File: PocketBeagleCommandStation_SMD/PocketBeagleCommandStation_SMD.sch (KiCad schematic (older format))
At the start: 37 parts, among them J1 Console, J2 DCC Output to Tracks, J7 USB_A, P1 POCKETBEAGLE-P1, P2 POCKETBEAGLE-P2, T1 DCC Power In, U11 INA2180A1IDGKR

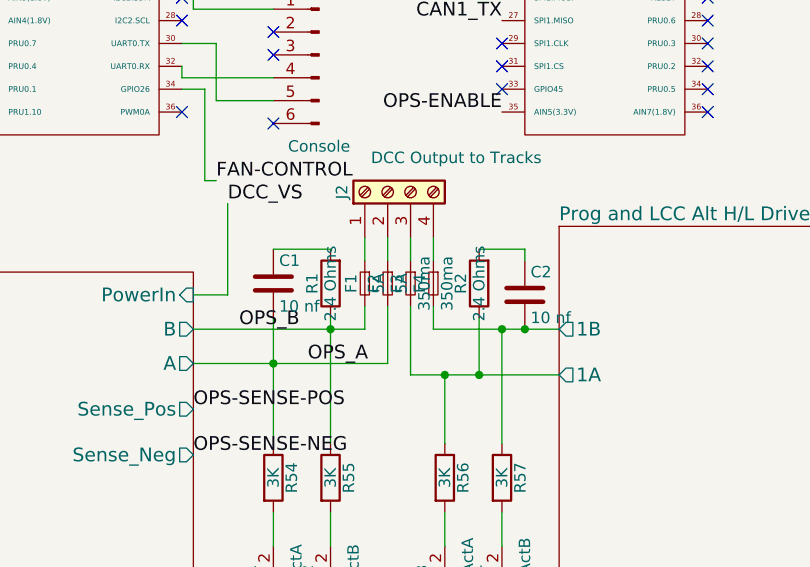
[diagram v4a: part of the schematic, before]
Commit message: continuing work on PocketBeagleCommandStation_SMD.
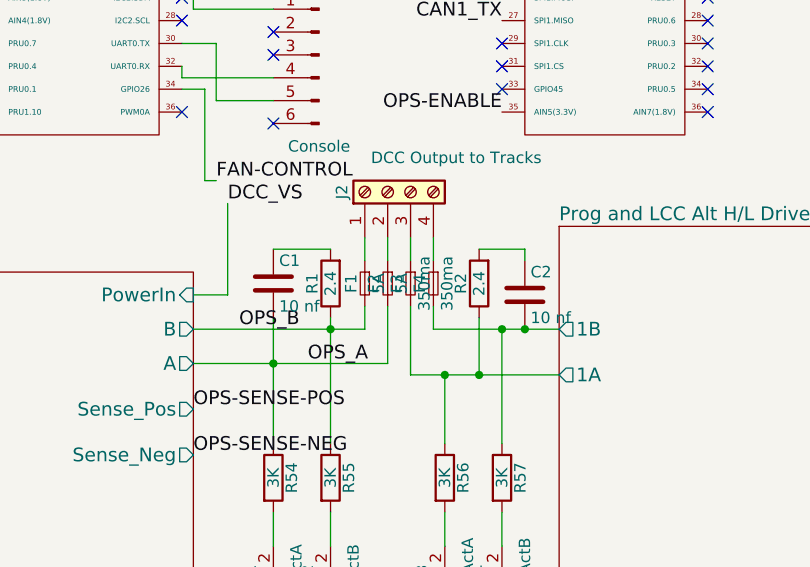
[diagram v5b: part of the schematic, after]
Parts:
- R1, R2: value 2.4 Ohms -> 2.4; footprint Resistors_THT:R_Axial_DIN0204_L3.6mm_D1.6mm_P2.54mm_Vertical -> Resistors_SMD:R_1206; Part Number 603-CFR-25JB-52-2R4 -> 71-CRCW12062R40FKEA
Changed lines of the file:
@@
 P 3950 4100
 F 0 "R1" V 4030 4100 50  0000 C CNN
-F 1 "2.4 Ohms" V 3950 4100 50  0000 C CNN
-F 2 "Resistors_THT:R_Axial_DIN0204_L3.6mm_D1.6mm_P2.54mm_Vertical" V 3880 4100 50  0001 C CNN
+F 1 "2.4" V 3950 4100 50  0000 C CNN
+F 2 "Resistors_SMD:R_1206" V 3880 4100 50  0001 C CNN
 F 3 "" H 3950 4100 50  0001 C CNN
-F 4 "603-CFR-25JB-52-2R4" V 3950 4100 60  0001 C CNN "Part Number"
+F 4 "71-CRCW12062R40FKEA" V 3950 4100 60  0001 C CNN "Part Number"
 	1    3950 4100
 	-1   0    0    1
@@
 P 4600 4100
 F 0 "R2" V 4680 4100 50  0000 C CNN
-F 1 "2.4 Ohms" V 4600 4100 50  0000 C CNN
-F 2 "Resistors_THT:R_Axial_DIN0204_L3.6mm_D1.6mm_P2.54mm_Vertical" V 4530 4100 50  0001 C CNN
+F 1 "2.4" V 4600 4100 50  0000 C CNN
+F 2 "Resistors_SMD:R_1206" V 4530 4100 50  0001 C CNN
 F 3 "" H 4600 4100 50  0001 C CNN
-F 4 "603-CFR-25JB-52-2R4" V 4600 4100 60  0001 C CNN "Part Number"
+F 4 "71-CRCW12062R40FKEA" V 4600 4100 60  0001 C CNN "Part Number"
 	1    4600 4100
 	-1   0    0    1

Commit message: Continuing work on PocketBeagleCommandStation_SMD.
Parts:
- added FID1, FID2, FID3: Fiducial, Fiducials:Fiducial_Modern_CopperTop, symbol Mounting_Hole
- added MK1, MK3, MK4: Mounting_Hole, Mounting_Holes:MountingHole_3.2mm_M3, symbol Mounting_Hole
- added MK2: Mounting_Hole_PAD, Mounting_Holes:MountingHole_3.2mm_M3_Pad_Via, symbol Mounting_Hole_PAD
- R48: footprint (none) -> Resistors_SMD:R_0603; Mouser Part Number (none) -> 667-ERJ-3EKF2401V
- R49: footprint (none) -> Resistors_SMD:R_0603; Mouser Part Number (none) -> 667-ERJ-3EKF1022V
- R50, R51: footprint (none) -> Resistors_SMD:R_0603; Mouser Part Number (none) -> 652-CR0603FX-1372ELF
- R52: footprint (none) -> Resistors_SMD:R_0603; Mouser Part  Number (none) -> 667-ERJ-3EKF1022V
- R53: value 2.4K Ohms -> 2.4K; footprint (none) -> Resistors_SMD:R_0603; Mouser Part Number (none) -> 667-ERJ-3EKF2401V
- R54, R55, R56, R57: footprint (none) -> Resistors_SMD:R_0603; Mouser Part Number (none) -> 660-RN73H1JT3001F100
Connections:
- net GND: now also MK2.1
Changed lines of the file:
@@
 F 0 "R51" V 5680 1000 50  0000 C CNN
 F 1 "13.7K" V 5600 1000 50  0000 C CNN
-F 2 "" V 5530 1000 50  0001 C CNN
+F 2 "Resistors_SMD:R_0603" V 5530 1000 50  0001 C CNN
 F 3 "" H 5600 1000 50  0001 C CNN
+F 4 "652-CR0603FX-1372ELF" V 5600 1000 60  0001 C CNN "Mouser Part Number"
 	1    5600 1000
 	0    1    1    0
@@
 F 0 "R52" V 5880 1200 50  0000 C CNN
 F 1 "10.2K" V 5800 1200 50  0000 C CNN
-F 2 "" V 5730 1200 50  0001 C CNN
+F 2 "Resistors_SMD:R_0603" V 5730 1200 50  0001 C CNN
 F 3 "" H 5800 1200 50  0001 C CNN
+F 4 "667-ERJ-3EKF1022V" V 5800 1200 60  0001 C CNN "Mouser Part  Number"
 	1    5800 1200
 	1    0    0    -1
@@
 P 6200 1000
 F 0 "R53" V 6280 1000 50  0000 C CNN
-F 1 "2.4K Ohms" V 6200 1000 50  0000 C CNN
-F 2 "" V 6130 1000 50  0001 C CNN
+F 1 "2.4K" V 6200 1000 50  0000 C CNN
+F 2 "Resistors_SMD:R_0603" V 6130 1000 50  0001 C CNN
 F 3 "" H 6200 1000 50  0001 C CNN
+F 4 "667-ERJ-3EKF2401V" V 6200 1000 60  0001 C CNN "Mouser Part Number"
 	1    6200 1000
 	0    1    1    0
@@
 F 0 "R50" V 3730 900 50  0000 C CNN
 F 1 "13.7K" V 3650 900 50  0000 C CNN
-F 2 "" V 3580 900 50  0001 C CNN
+F 2 "Resistors_SMD:R_0603" V 3580 900 50  0001 C CNN
 F 3 "" H 3650 900 50  0001 C CNN
+F 4 "652-CR0603FX-1372ELF" V 3650 900 60  0001 C CNN "Mouser Part Number"
 	1    3650 900
 	0    1    1    0
@@
 F 0 "R48" V 3180 900 50  0000 C CNN
 F 1 "2.4K" V 3100 900 50  0000 C CNN
-F 2 "" V 3030 900 50  0001 C CNN
+F 2 "Resistors_SMD:R_0603" V 3030 900 50  0001 C CNN
 F 3 "" H 3100 900 50  0001 C CNN
+F 4 "667-ERJ-3EKF2401V" V 3100 900 60  0001 C CNN "Mouser Part Number"
 	1    3100 900
 	0    1    1    0
@@
 F 0 "R49" V 3530 1100 50  0000 C CNN
 F 1 "10.2K" V 3450 1100 50  0000 C CNN
-F 2 "" V 3380 1100 50  0001 C CNN
+F 2 "Resistors_SMD:R_0603" V 3380 1100 50  0001 C CNN
 F 3 "" H 3450 1100 50  0001 C CNN
+F 4 "667-ERJ-3EKF1022V" V 3450 1100 60  0001 C CNN "Mouser Part Number"
 	1    3450 1100
 	1    0    0    -1
@@
 F 0 "R54" V 3780 4950 50  0000 C CNN
 F 1 "3K" V 3700 4950 50  0000 C CNN
-F 2 "" V 3630 4950 50  0001 C CNN
+F 2 "Resistors_SMD:R_0603" V 3630 4950 50  0001 C CNN
 F 3 "" H 3700 4950 50  0001 C CNN
+F 4 "660-RN73H1JT3001F100" V 3700 4950 60  0001 C CNN "Mouser Part Number"
 	1    3700 4950
 	1    0    0    -1
@@
 F 0 "R55" V 4030 4950 50  0000 C CNN
 F 1 "3K" V 3950 4950 50  0000 C CNN
-F 2 "" V 3880 4950 50  0001 C CNN
+F 2 "Resistors_SMD:R_0603" V 3880 4950 50  0001 C CNN
 F 3 "" H 3950 4950 50  0001 C CNN
+F 4 "660-RN73H1JT3001F100" V 3950 4950 60  0001 C CNN "Mouser Part Number"
 	1    3950 4950
 	1    0    0    -1
@@
 F 0 "R56" V 4530 4950 50  0000 C CNN
 F 1 "3K" V 4450 4950 50  0000 C CNN
-F 2 "" V 4380 4950 50  0001 C CNN
+F 2 "Resistors_SMD:R_0603" V 4380 4950 50  0001 C CNN
 F 3 "" H 4450 4950 50  0001 C CNN
+F 4 "660-RN73H1JT3001F100" V 4450 4950 60  0001 C CNN "Mouser Part Number"
 	1    4450 4950
 	1    0    0    -1
@@
 F 0 "R57" V 4780 4950 50  0000 C CNN
 F 1 "3K" V 4700 4950 50  0000 C CNN
-F 2 "" V 4630 4950 50  0001 C CNN
+F 2 "Resistors_SMD:R_0603" V 4630 4950 50  0001 C CNN
 F 3 "" H 4700 4950 50  0001 C CNN
+F 4 "660-RN73H1JT3001F100" V 4700 4950 60  0001 C CNN "Mouser Part Number"
 	1    4700 4950
 	1    0    0    -1
@@
 	5400 700  5250 700
 Wire Wire Line
-	4150 1000 4000 1000
+	4000 1000 4150 1000
 Wire Wire Line
 	4150 900  3800 900
@@
 Wire Wire Line
 	10250 1650 10250 1250
+$Comp
+L Mounting_Hole MK3
+U 1 1 607774AA
+P 5300 7850
+F 0 "MK3" H 5300 8050 50  0000 C CNN
+F 1 "Mounting_Hole" H 5300 7975 50  0000 C CNN
+F 2 "Mounting_Holes:MountingHole_3.2mm_M3" H 5300 7850 50  0001 C CNN
+F 3 "" H 5300 7850 50  0001 C CNN
+	1    5300 7850
+	1    0    0    -1
+$EndComp
+$Comp
+L Mounting_Hole MK1
+U 1 1 6077776D
+P 5950 7150
+F 0 "MK1" H 5950 7350 50  0000 C CNN
+F 1 "Mounting_Hole" H 5950 7275 50  0000 C CNN
+F 2 "Mounting_Holes:MountingHole_3.2mm_M3" H 5950 7150 50  0001 C CNN
+F 3 "" H 5950 7150 50  0001 C CNN
+	1    5950 7150
+	1    0    0    -1
+$EndComp
+$Comp
+L Mounting_Hole MK4
+U 1 1 60777A2E
+P 5950 7850
+F 0 "MK4" H 5950 8050 50  0000 C CNN
+F 1 "Mounting_Hole" H 5950 7975 50  0000 C CNN
+F 2 "Mounting_Holes:MountingHole_3.2mm_M3" H 5950 7850 50  0001 C CNN
+F 3 "" H 5950 7850 50  0001 C CNN
+	1    5950 7850
+	1    0    0    -1
+$EndComp
+$Comp
+L Mounting_Hole_PAD MK2
+U 1 1 60777C47
+P 5300 7200
+F 0 "MK2" H 5300 7450 50  0000 C CNN
+F 1 "Mounting_Hole_PAD" H 5300 7375 50  0000 C CNN
+F 2 "Mounting_Holes:MountingHole_3.2mm_M3_Pad_Via" H 5300 7200 50  0001 C CNN
+F 3 "" H 5300 7200 50  0001 C CNN
+	1    5300 7200
+	1    0    0    -1
+$EndComp
+$Comp
+L GND #PWR018
+U 1 1 607784BF
+P 5300 7350
+F 0 "#PWR018" H 5300 7100 50  0001 C CNN
+F 1 "GND" H 5300 7200 50  0000 C CNN
+F 2 "" H 5300 7350 50  0001 C CNN
+F 3 "" H 5300 7350 50  0001 C CNN
+	1    5300 7350
+	1    0    0    -1
+$EndComp
+$Comp
+L Mounting_Hole FID1
+U 1 1 60778AC3
+P 4000 7850
+F 0 "FID1" H 4000 8050 50  0000 C CNN
+F 1 "Fiducial" H 4000 7975 50  0000 C CNN
+F 2 "Fiducials:Fiducial_Modern_CopperTop" H 4000 7850 50  0001 C CNN
+F 3 "" H 4000 7850 50  0001 C CNN
+	1    4000 7850
+	1    0    0    -1
+$EndComp
+$Comp
+L Mounting_Hole FID2
+U 1 1 60778C48
+P 4400 7850
+F 0 "FID2" H 4400 8050 50  0000 C CNN
+F 1 "Fiducial" H 4400 7975 50  0000 C CNN
+F 2 "Fiducials:Fiducial_Modern_CopperTop" H 4400 7850 50  0001 C CNN
+F 3 "" H 4400 7850 50  0001 C CNN
+	1    4400 7850
+	1    0    0    -1
+$EndComp
+$Comp
+L Mounting_Hole FID3
+U 1 1 60778DBB
+P 4800 7850
+F 0 "FID3" H 4800 8050 50  0000 C CNN
+F 1 "Fiducial" H 4800 7975 50  0000 C CNN
+F 2 "Fiducials:Fiducial_Modern_CopperTop" H 4800 7850 50  0001 C CNN
+F 3 "" H 4800 7850 50  0001 C CNN
+	1    4800 7850
+	1    0    0    -1
+$EndComp
+Wire Wire Line
+	5300 7300 5300 7350
 $EndSCHEMATC

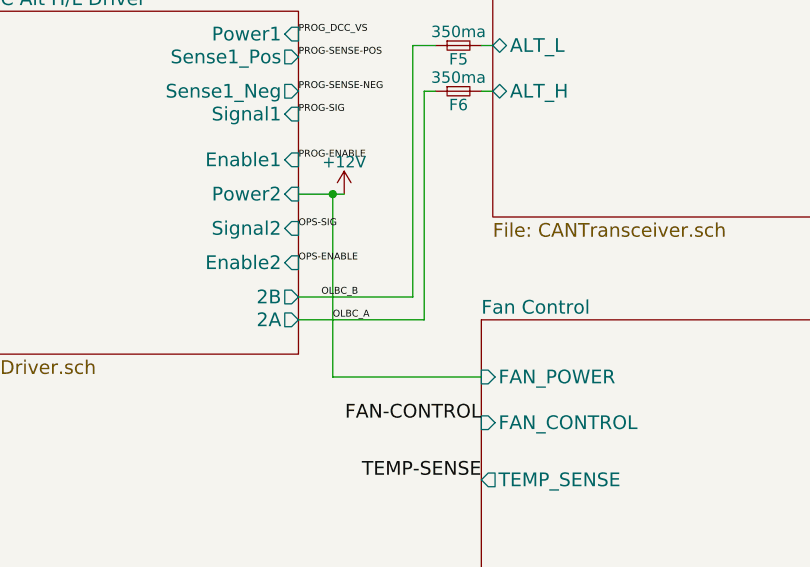
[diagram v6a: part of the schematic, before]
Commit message: Almost done: just the Rail Com section to go.
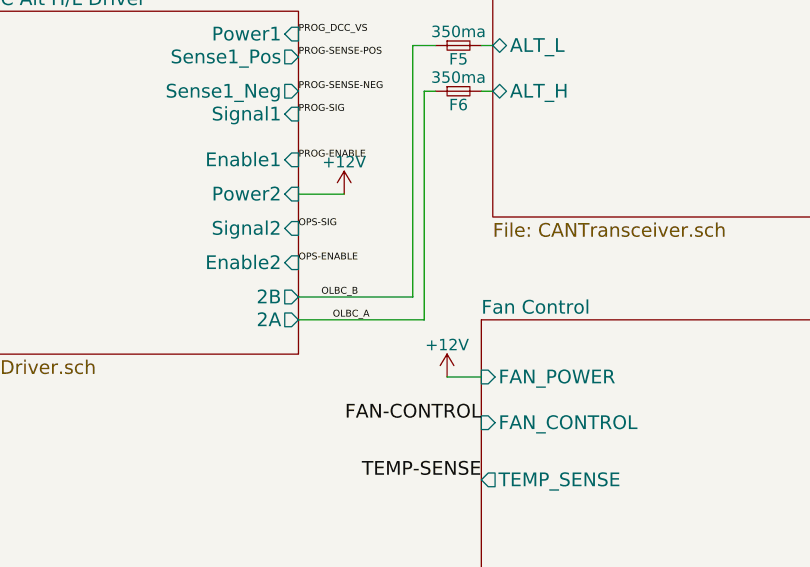
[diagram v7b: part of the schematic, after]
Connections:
- net +12V: no longer F6.1
- new net OLBC_A: F6.1
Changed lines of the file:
@@
 	6750 4650 6950 4650
-Wire Wire Line
-	6900 4650 6900 5450
-Wire Wire Line
-	6900 5450 7550 5450
-Connection ~ 6900 4650
 Wire Wire Line
 	3950 4250 3950 4800
@@
 Wire Wire Line
 	5300 7300 5300 7350
+$Comp
+L +12V #PWR019
+U 1 1 60774528
+P 7400 5450
+F 0 "#PWR019" H 7400 5300 50  0001 C CNN
+F 1 "+12V" H 7400 5590 50  0000 C CNN
+F 2 "" H 7400 5450 50  0001 C CNN
+F 3 "" H 7400 5450 50  0001 C CNN
+	1    7400 5450
+	1    0    0    -1
+$EndComp
+Wire Wire Line
+	7550 5450 7400 5450
 $EndSCHEMATC

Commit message: Minor fixes (cleaning up extra fields in the schematic).
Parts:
- C1, C2: Mouser Part Number (none) -> 791-1206B103K500CT; Part Number 791-1206B103K500CT -> (none)
- J2: Mouser Part Number (none) -> 651-5442264; Part Number 651-5442264 -> (none)
- R1, R2: Mouser Part Number (none) -> 71-CRCW12062R40FKEA; Part Number 71-CRCW12062R40FKEA -> (none)
- R52: Mouser Part  Number 667-ERJ-3EKF1022V -> (none); Mouser Part Number (none) -> 667-ERJ-3EKF1022V
- T1: Mouser Part Number (none) -> 651-5442251; Part Number 651-5442251 -> (none)
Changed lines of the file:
@@
 F 2 "Connectors_Terminal_Blocks:TerminalBlock_Pheonix_PT-3.5mm_3pol" H 6950 1750 50  0001 C CNN
 F 3 "" H 6950 1750 50  0001 C CNN
-F 4 "651-5442251" H 6950 1750 60  0001 C CNN "Part Number"
+F 4 "651-5442251" H 6950 1750 60  0001 C CNN "Mouser Part Number"
 	1    6950 1750
 	-1   0    0    -1
@@
 F 2 "Connectors_Terminal_Blocks:TerminalBlock_Pheonix_PT-3.5mm_4pol" H 4200 3700 50  0001 C CNN
 F 3 "" H 4200 3700 50  0001 C CNN
-F 4 "651-5442264" H 4200 3700 60  0001 C CNN "Part Number"
+F 4 "651-5442264" H 4200 3700 60  0001 C CNN "Mouser Part Number"
 	1    4200 3700
 	0    -1   -1   0
@@
 F 2 "Resistors_SMD:R_1206" V 3880 4100 50  0001 C CNN
 F 3 "" H 3950 4100 50  0001 C CNN
-F 4 "71-CRCW12062R40FKEA" V 3950 4100 60  0001 C CNN "Part Number"
+F 4 "71-CRCW12062R40FKEA" V 3950 4100 60  0001 C CNN "Mouser Part Number"
 	1    3950 4100
 	-1   0    0    1
@@
 F 2 "Capacitors_SMD:C_1206" H 3738 3950 50  0001 C CNN
 F 3 "" H 3700 4100 50  0001 C CNN
-F 4 "791-1206B103K500CT" H 3700 4100 60  0001 C CNN "Part Number"
+F 4 "791-1206B103K500CT" H 3700 4100 60  0001 C CNN "Mouser Part Number"
 	1    3700 4100
 	1    0    0    -1
@@
 F 2 "Resistors_SMD:R_1206" V 4530 4100 50  0001 C CNN
 F 3 "" H 4600 4100 50  0001 C CNN
-F 4 "71-CRCW12062R40FKEA" V 4600 4100 60  0001 C CNN "Part Number"
+F 4 "71-CRCW12062R40FKEA" V 4600 4100 60  0001 C CNN "Mouser Part Number"
 	1    4600 4100
 	-1   0    0    1
@@
 F 2 "Capacitors_SMD:C_1206" H 4838 4000 50  0001 C CNN
 F 3 "" H 4800 4150 50  0001 C CNN
-F 4 "791-1206B103K500CT" H 4800 4150 60  0001 C CNN "Part Number"
+F 4 "791-1206B103K500CT" H 4800 4150 60  0001 C CNN "Mouser Part Number"
 	1    4800 4150
 	1    0    0    -1
@@
 F 2 "Resistors_SMD:R_0603" V 5730 1200 50  0001 C CNN
 F 3 "" H 5800 1200 50  0001 C CNN
-F 4 "667-ERJ-3EKF1022V" V 5800 1200 60  0001 C CNN "Mouser Part  Number"
+F 4 "667-ERJ-3EKF1022V" V 5800 1200 60  0001 C CNN "Mouser Part Number"
 	1    5800 1200
 	1    0    0    -1
